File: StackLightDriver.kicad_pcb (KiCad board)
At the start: 2 copper layers, 100 x 100 mm, 99 parts, among them J1 B2B-XH-A, J10 B2B-XH-A, J11 PJ-102AH, J12 USB_C_Receptacle_USB2.0_14P, J2 B2B-XH-A, J3 B2B-XH-A, J4 B2B-XH-A, J5 B2B-XH-A, J6 B2B-XH-A, J7 B2B-XH-A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

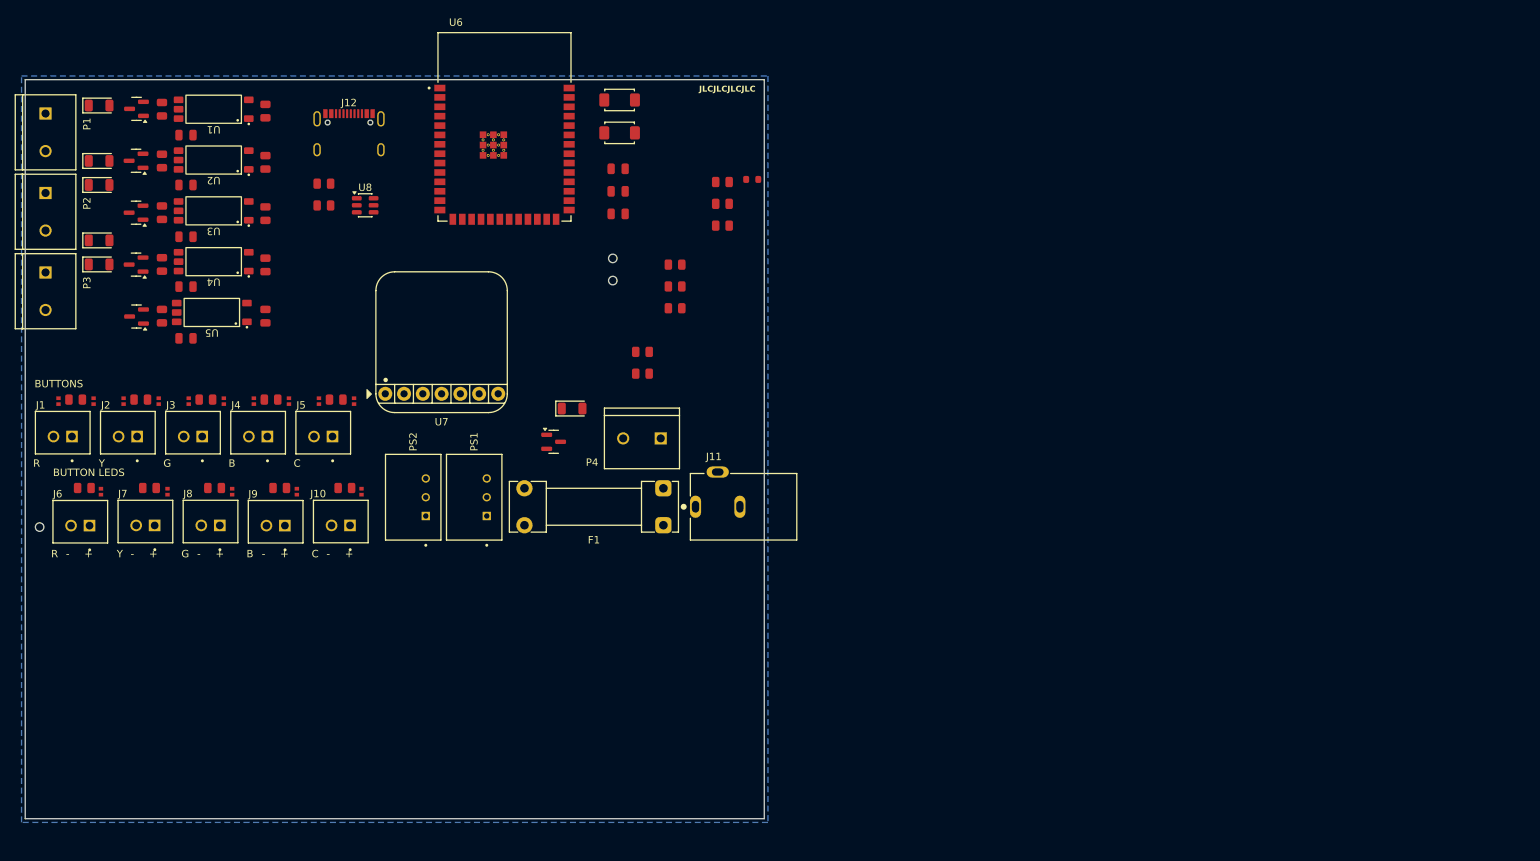
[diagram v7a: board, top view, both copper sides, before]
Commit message: First routing attempt
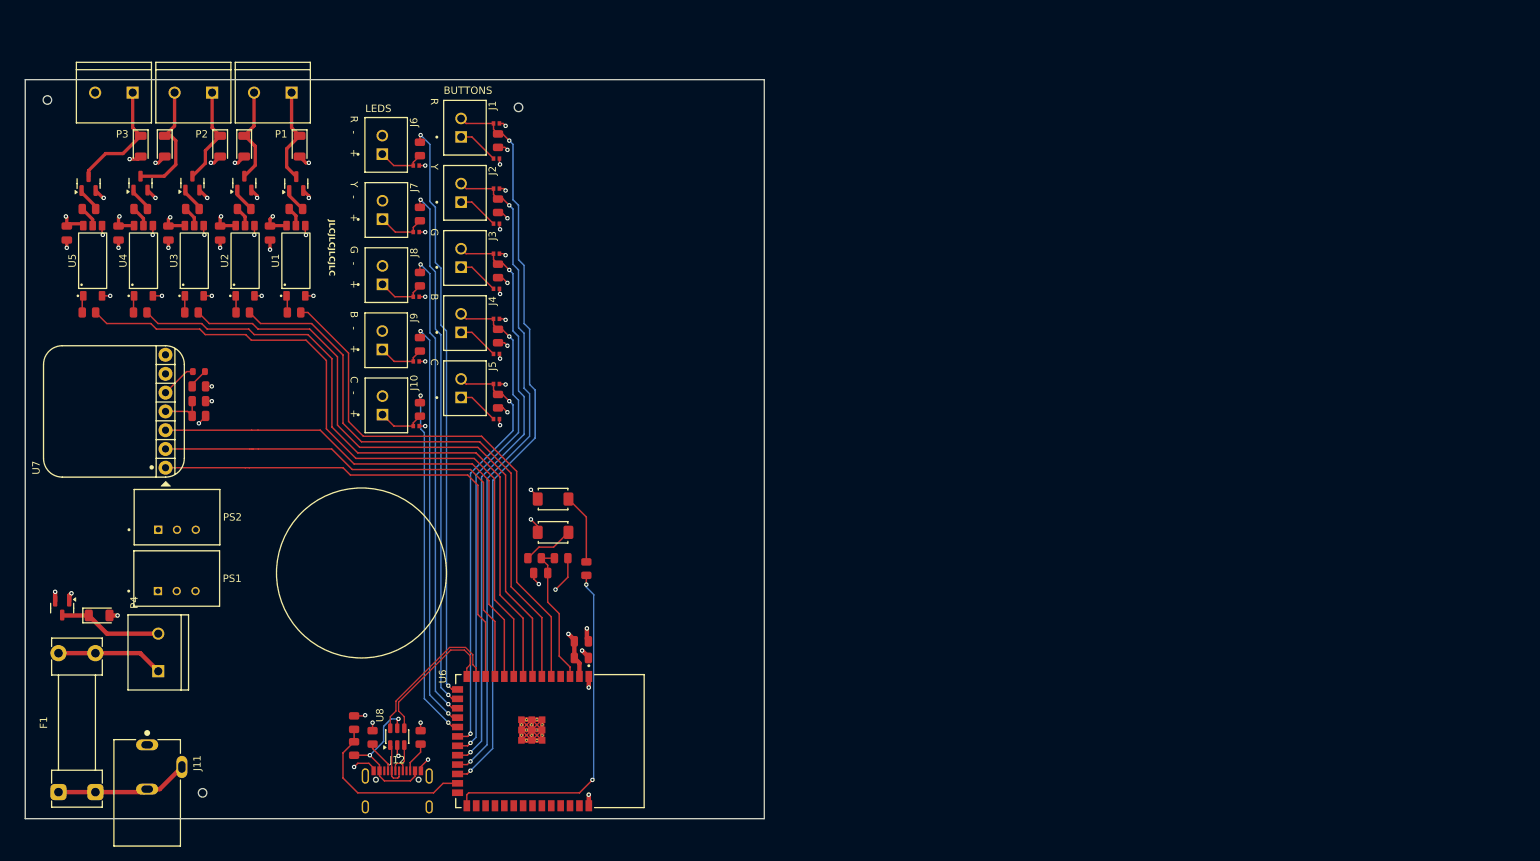
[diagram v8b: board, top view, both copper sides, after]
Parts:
- moved J11 89.5 mm to (75.5, 130.5), turned to -90 degrees
- moved F1 89.5 mm to (63.5, 130.4), turned to 90 degrees
- moved J12 89.2 mm to (109.3, 132.4)
- moved U6 83.3 mm to (130.0, 123.5), turned to -90 degrees
- moved H3 80.3 mm to (62.0, 36.8)
- moved R27 79.3 mm to (82.5, 73.5), turned to 180 degrees
- moved R24 76.8 mm to (82.5, 77.5), turned to 180 degrees
- moved R30 76.5 mm to (103.5, 124.5), turned to 90 degrees
- moved R25 76.4 mm to (82.5, 79.5)
- moved R26 74.1 mm to (82.5, 75.5), turned to 180 degrees
- moved U8 72.0 mm to (109.3, 122.9), turned to 90 degrees
- moved P4 71.6 mm to (77.0, 111.5), turned to 90 degrees
- moved R29 71.0 mm to (106.0, 123.0), turned to 90 degrees
- moved Q6 70.2 mm to (64.0, 105.5), turned to -90 degrees
- moved D6 70.2 mm to (122.8, 39.9), turned to 180 degrees
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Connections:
- U6 pad 10: unconnected-(U6-IO17-Pad10) -> /DIN
- U6 pad 11: unconnected-(U6-IO18-Pad11) -> /BCLK
- U6 pad 12: unconnected-(U6-IO8-Pad12) -> /LRC
- U6 pad 15: unconnected-(U6-IO3-Pad15) -> /BUTTON_LED_RED
- U6 pad 16: unconnected-(U6-IO46-Pad16) -> /BUTTON_LED_YELLOW
- U6 pad 17: unconnected-(U6-IO9-Pad17) -> /BUTTON_LED_GREEN
- U6 pad 18: unconnected-(U6-IO10-Pad18) -> /BUTTON_LED_BLUE
- U6 pad 19: unconnected-(U6-IO11-Pad19) -> /BUTTON_LED_WHITE
- U6 pad 20: unconnected-(U6-IO12-Pad20) -> /BUTTON_WHITE
- U6 pad 21: unconnected-(U6-IO13-Pad21) -> /BUTTON_BLUE
- U6 pad 22: unconnected-(U6-IO14-Pad22) -> /BUTTON_GREEN
- U6 pad 23: unconnected-(U6-IO21-Pad23) -> /BUTTON_YELLOW
- U6 pad 24: unconnected-(U6-IO47-Pad24) -> /BUTTON_RED
- U6 pad 25: unconnected-(U6-IO48-Pad25) -> /USB_POWER_IN_SIGNAL
- U6 pad 41_10: (no net) -> GND
- U6 pad 41_11: (no net) -> GND
- U6 pad 41_12: (no net) -> GND
- U6 pad 41_13: (no net) -> GND
- U6 pad 41_14: (no net) -> GND
- U6 pad 41_15: (no net) -> GND
- U6 pad 41_16: (no net) -> GND
- U6 pad 41_17: (no net) -> GND
- U6 pad 41_18: (no net) -> GND
- U6 pad 41_19: (no net) -> GND
- U6 pad 41_20: (no net) -> GND
- U6 pad 41_21: (no net) -> GND
- U6 pad 5: unconnected-(U6-IO5-Pad5) -> /LED_RED
- U6 pad 6: unconnected-(U6-IO6-Pad6) -> /LED_YELLOW
- U6 pad 7: unconnected-(U6-IO7-Pad7) -> /LED_GREEN
- U6 pad 8: unconnected-(U6-IO15-Pad8) -> /LED_BLUE
- U6 pad 9: unconnected-(U6-IO16-Pad9) -> /LED_WHITE
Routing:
- net GND: track 0.00 -> 104.3 mm, vias 0 -> 56
- net /BUTTON_RED: track 0.00 -> 100.5 mm, vias 0 -> 2
- net /LED_WHITE: track 0.00 -> 96.5 mm
- net /LED_BLUE: track 0.00 -> 90.7 mm
- net /BUTTON_YELLOW: track 0.00 -> 89.9 mm, vias 0 -> 2
- net /LED_GREEN: track 0.00 -> 84.9 mm
- net /BUTTON_GREEN: track 0.00 -> 79.2 mm, vias 0 -> 2
- net /LED_YELLOW: track 0.00 -> 79.1 mm
- net /BUTTON_LED_RED: track 0.00 -> 78.5 mm, vias 0 -> 2
- net /DIN: track 0.00 -> 74.0 mm
- net /LED_RED: track 0.00 -> 73.2 mm
- net /BCLK: track 0.00 -> 71.8 mm
- net /BUTTON_LED_YELLOW: track 0.00 -> 71.1 mm, vias 0 -> 2
- net /LRC: track 0.00 -> 69.6 mm
- net /BUTTON_BLUE: track 0.00 -> 68.4 mm, vias 0 -> 2
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- added copper zone on In1.Cu, net GND
- added copper zone on In2.Cu, net VAMP
- added copper zone on In2.Cu, net VMCU
- added copper zone on In2.Cu, net VSupply
- removed copper zone on B.Cu, net GND
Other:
- copper layers 2 -> 4
- board text added: "LEDS"
- board text added: "Switch goes here"
- board text removed: "BUTTON LEDS"
